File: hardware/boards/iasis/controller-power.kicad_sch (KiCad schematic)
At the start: 10 parts, among them U1181 74HC595PW, U1182 74HC595PW

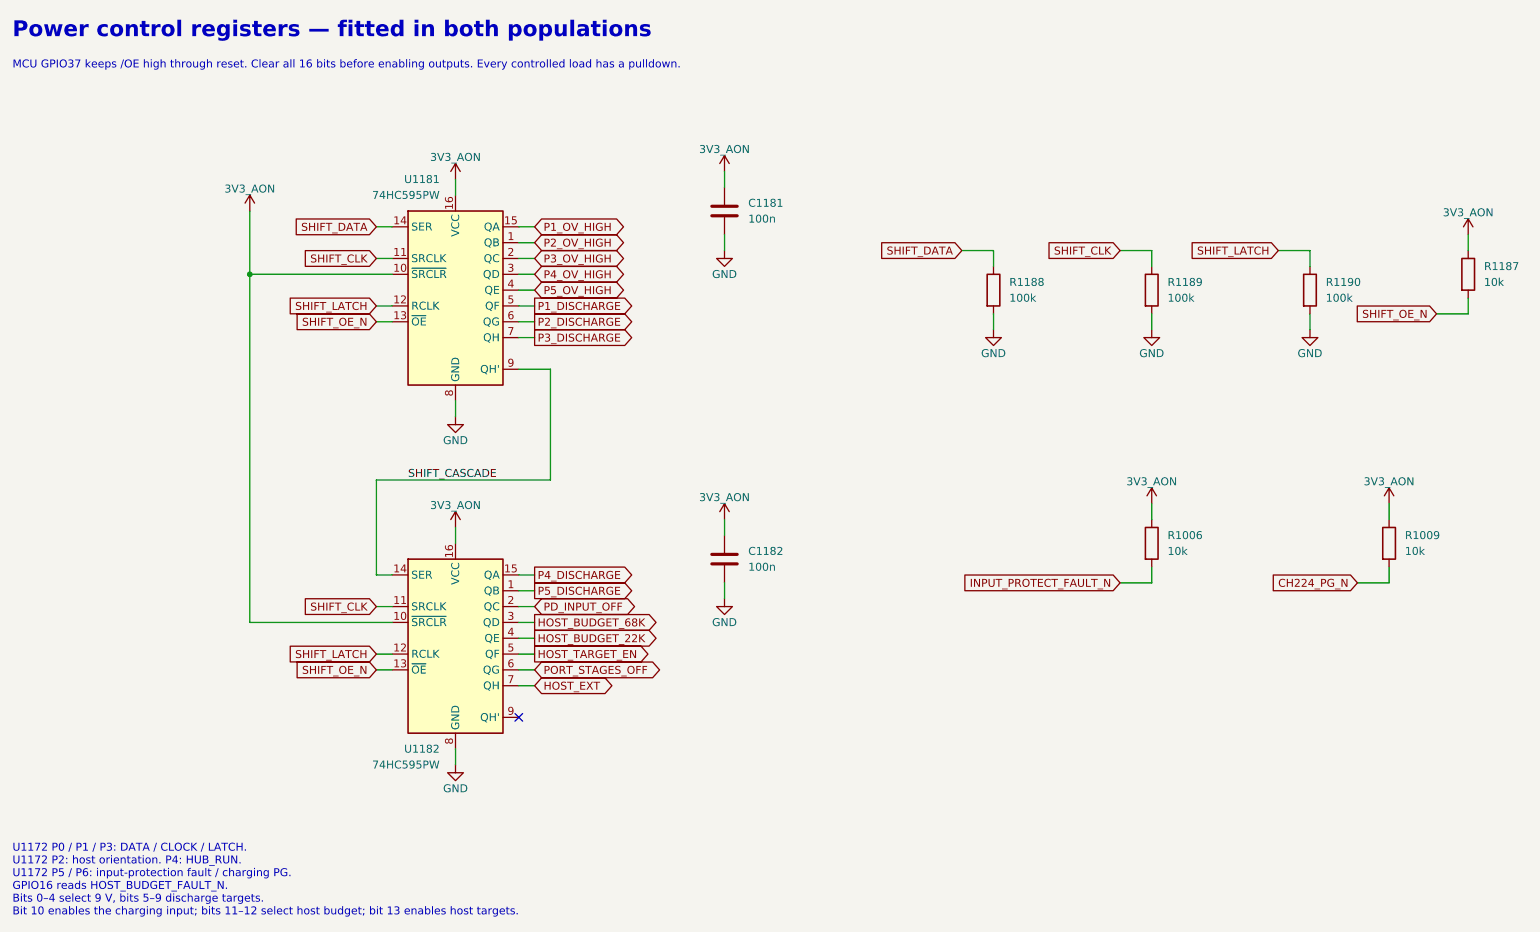
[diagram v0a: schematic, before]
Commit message: feat(hardware): group shift-register outputs by direction
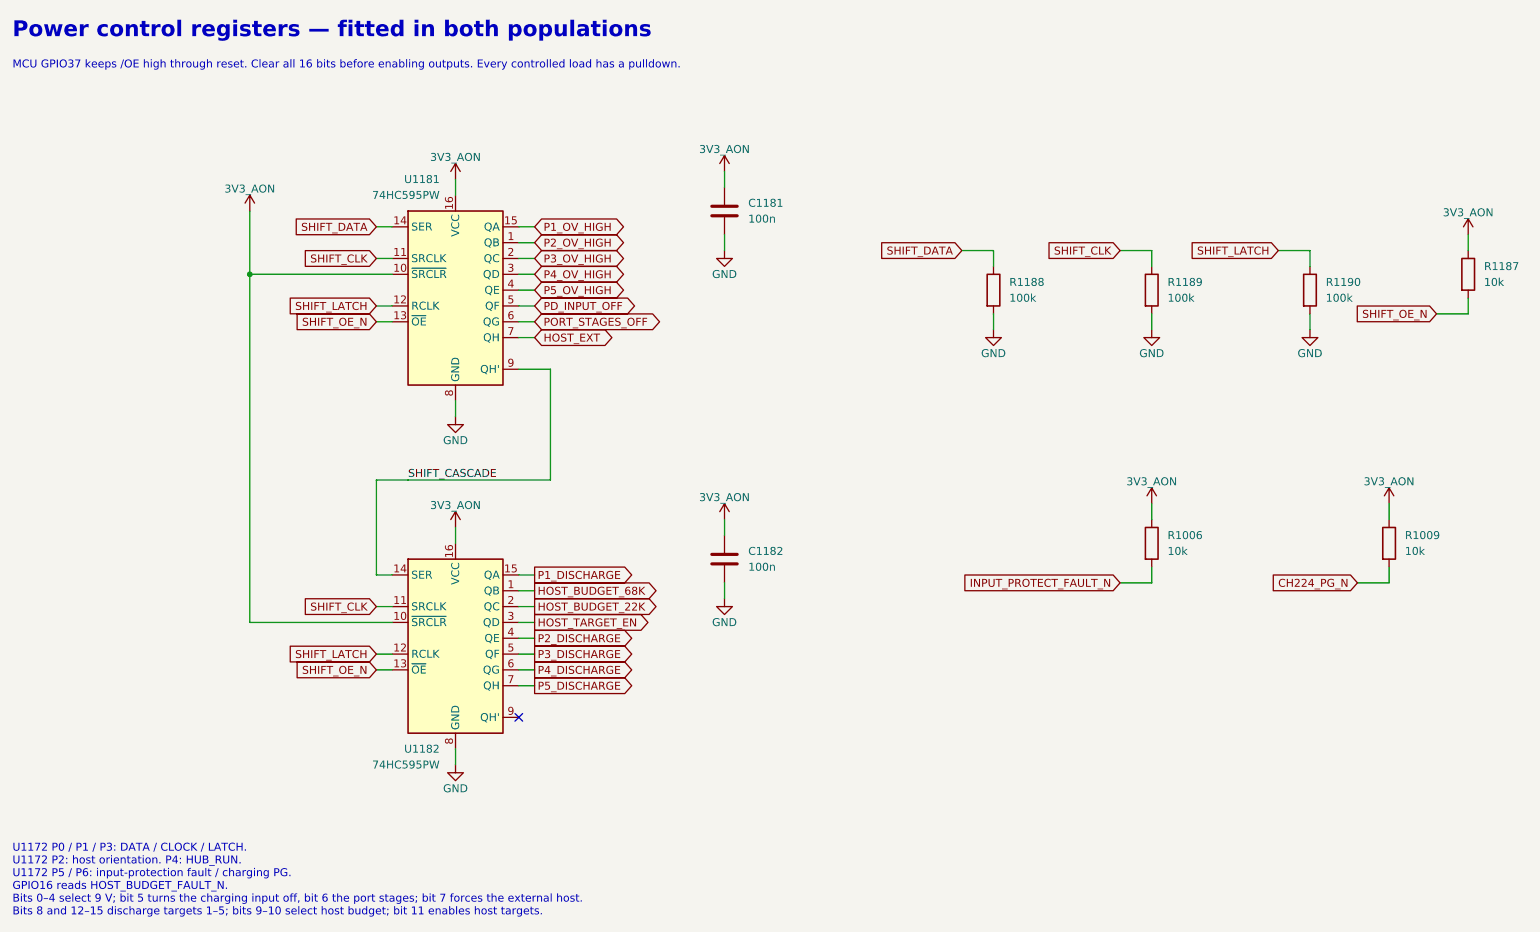
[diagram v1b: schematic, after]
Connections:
- net HOST_BUDGET_22K: now also U1182.2 (QC); no longer U1182.4 (QE)
- net HOST_BUDGET_68K: now also U1182.1 (QB); no longer U1182.3 (QD)
- net HOST_EXT: now also U1181.7 (QH); no longer U1182.7 (QH)
- net HOST_TARGET_EN: now also U1182.3 (QD); no longer U1182.5 (QF)
- net P1_DISCHARGE: now also U1182.15 (QA); no longer U1181.5 (QF)
- net P2_DISCHARGE: now also U1182.4 (QE); no longer U1181.6 (QG)
- net P3_DISCHARGE: now also U1182.5 (QF); no longer U1181.7 (QH)
- net P4_DISCHARGE: now also U1182.6 (QG); no longer U1182.15 (QA)
- net P5_DISCHARGE: now also U1182.7 (QH); no longer U1182.1 (QB)
- net PD_INPUT_OFF: now also U1181.5 (QF); no longer U1182.2 (QC)
- net PORT_STAGES_OFF: now also U1181.6 (QG); no longer U1182.6 (QG)
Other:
- note added: "U1172 P0 / P1 / P3: DATA / CLOCK / LATCH. U1172 P2: host orientation. P4: HUB_RUN. U1172 P5 / P6: input-protection fault / charging PG. GPIO16 reads HOST_BUDGET_FAULT_N. Bits 0–4 select 9 V; bit 5 turns the charging input off, bit 6 the port stages; bit 7 forces the external host. Bits 8 and 12–15 discharge targets 1–5; bits 9–10 select host budget; bit 11 enables host targets."
- note removed: "U1172 P0 / P1 / P3: DATA / CLOCK / LATCH. U1172 P2: host orientation. P4: HUB_RUN. U1172 P5 / P6: input-protection fault / charging PG. GPIO16 reads HOST_BUDGET_FAULT_N. Bits 0–4 select 9 V, bits 5–9 discharge targets. Bit 10 enables the charging input; bits 11–12 select host budget; bit 13 enables host targets."
